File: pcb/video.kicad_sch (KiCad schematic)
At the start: 27 parts, among them J5 VGA, J6 SHIELD, Q4 2N7000, Q5 2N7000, Q6 2N7000, U11 74HC04, U12 74HC00, U13 4053, U14 74HC157, U15 74HC157, U16 74AC573, U17 74HC109, U18 74HC109, U2 74HC139, X1 25.175MHz

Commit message: update to kicad 10 and fix vertical video timing
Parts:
- removed unit 6 of U11
- renumbered R14 to R15, R15 to R16, R16 to R17, R17 to R18
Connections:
- no-connect marks 15 -> 14
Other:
- note added: "-796: HBlank off"
- note added: "Final column 0"
- note added: "Final line: -1"
- note added: "First column -799"
- note added: "First line: -525"
- note added: "HBlank on: -156"
- note added: "NOTE: Line 0 is skipped 74HC161 ~PE is not gated by CET/CEP"
- note added: "VBlank off: -520"
- note added: "VBlank on: -40"
- note removed: "-156"
- note removed: "-40"
- note removed: "-520"
- note removed: "-524"
- note removed: "-796"
- note removed: "-799"
- note removed: "0"

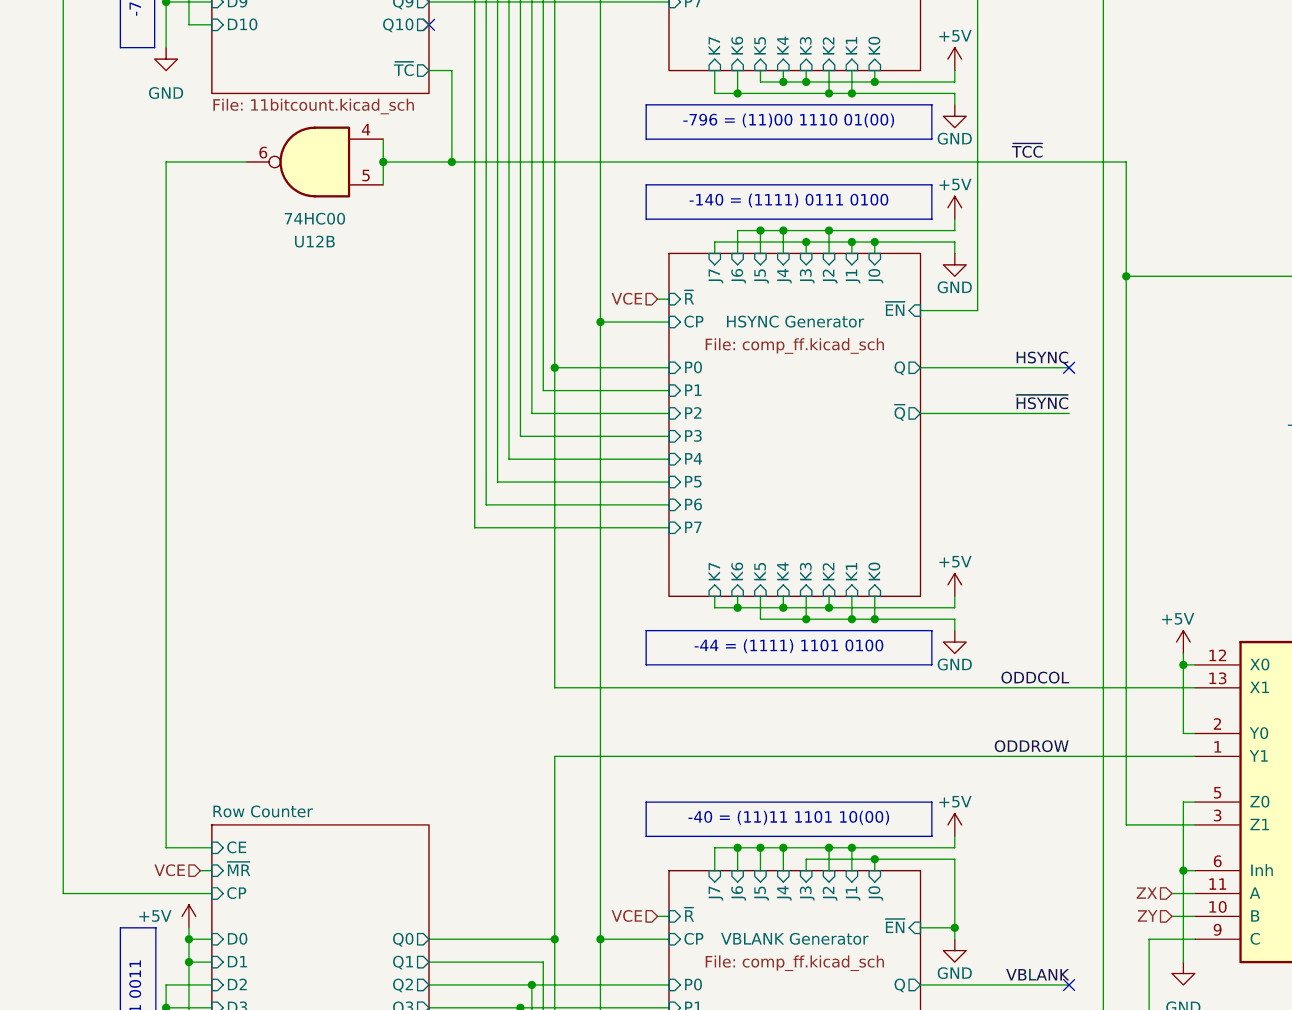
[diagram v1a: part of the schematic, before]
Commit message: fix y coordinate counter input polarity
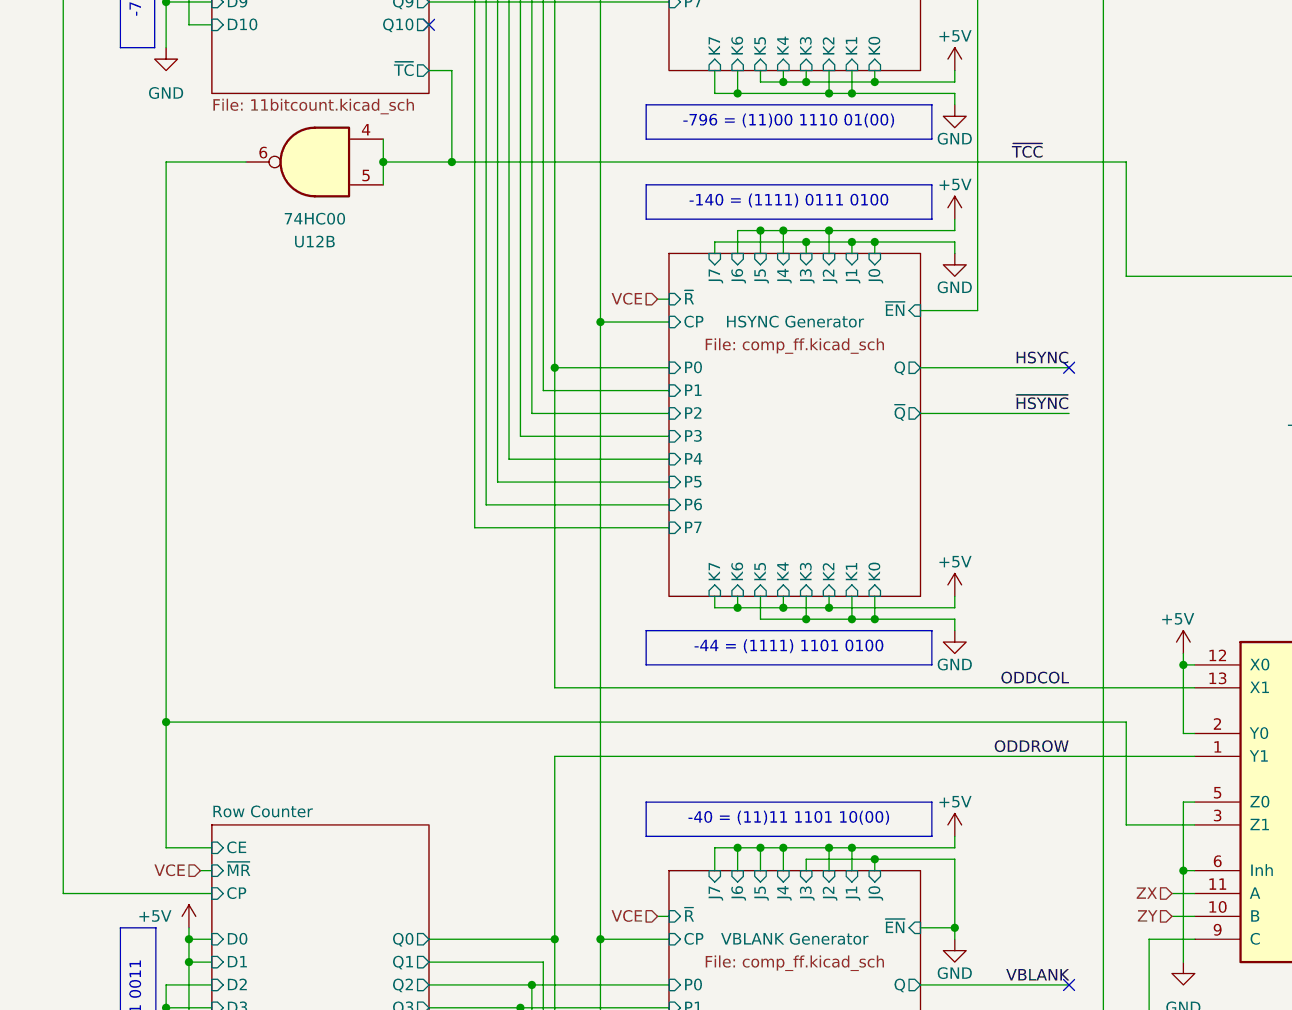
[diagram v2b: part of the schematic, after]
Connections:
- net Row Counter/CE: now also U13.3 (Z1)
- net ~{TCC}: no longer U13.3 (Z1)
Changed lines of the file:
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@@
 	)
 	(junction
-		(at 158.75 104.14)
-		(diameter 0)
-		(color 0 0 0 0)
-	)
-	(junction
 		(at 201.93 170.18)
 		(diameter 0)
@@
 	)
 	(junction
+		(at 52.07 153.67)
+		(diameter 0)
+		(color 0 0 0 0)
+	)
+	(junction
 		(at 384.81 220.98)
 		(diameter 0)
@@
 	(wire
 		(pts
+			(xy 158.75 165.1) (xy 158.75 153.67)
+		)
+		(stroke
+			(width 0)
+			(type default)
+		)
+	)
+	(wire
+		(pts
 			(xy 120.65 269.24) (xy 123.19 269.24)
 		)
@@
 	(wire
 		(pts
-			(xy 158.75 104.14) (xy 158.75 165.1)
-		)
-		(stroke
-			(width 0)
-			(type default)
-		)
-	)
-	(wire
-		(pts
 			(xy 125.73 140.97) (xy 125.73 139.7)
 		)
@@
 	(wire
 		(pts
+			(xy 52.07 153.67) (xy 52.07 167.64)
+		)
+		(stroke
+			(width 0)
+			(type default)
+		)
+	)
+	(wire
+		(pts
 			(xy 83.82 91.44) (xy 83.82 81.28)
 		)
@@
 	(wire
 		(pts
+			(xy 158.75 153.67) (xy 52.07 153.67)
+		)
+		(stroke
+			(width 0)
+			(type default)
+		)
+	)
+	(wire
+		(pts
 			(xy 118.11 226.06) (xy 128.27 226.06)
 		)
@@
 	(wire
 		(pts
-			(xy 52.07 91.44) (xy 52.07 167.64)
+			(xy 52.07 91.44) (xy 52.07 153.67)
 		)
 		(stroke
